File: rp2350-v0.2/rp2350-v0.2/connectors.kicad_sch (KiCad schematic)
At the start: 6 parts, among them J1 USB_C_Receptacle_USB2.0_14P, J2 SWD, J3 BAT, J5 DBG_UART

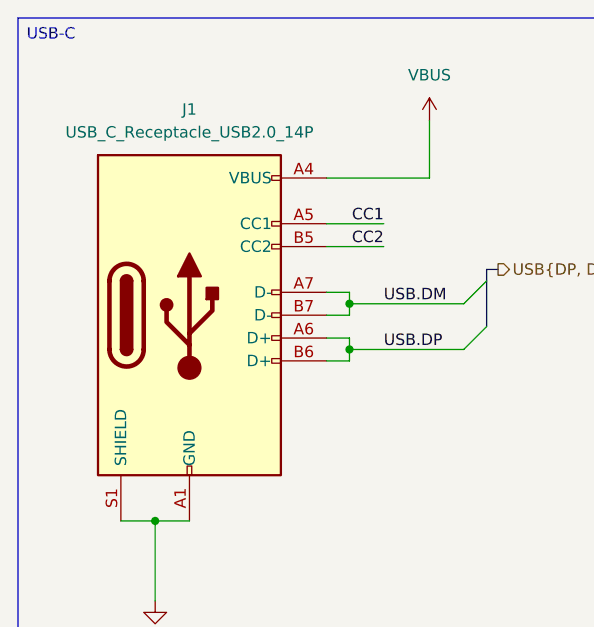
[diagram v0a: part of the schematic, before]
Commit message: v0.2: schematic draft 1 done
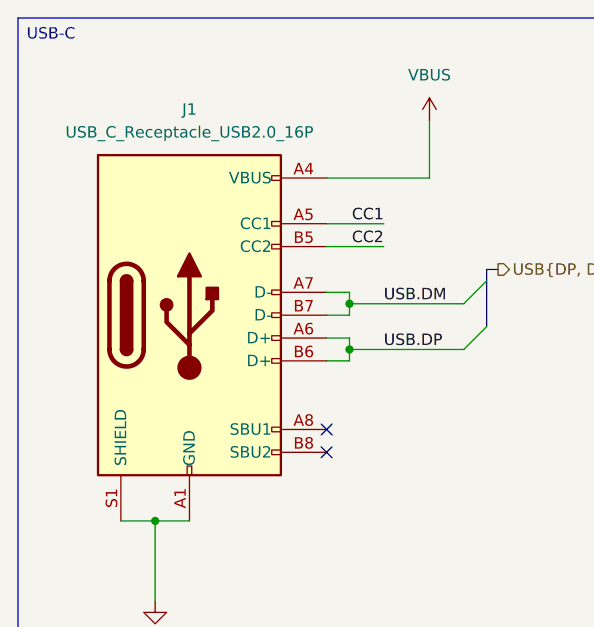
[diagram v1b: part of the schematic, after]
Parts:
- removed J1: USB_C_Receptacle_USB2.0_14P, symbol Connector:USB_C_Receptacle_USB2.0_14P
- added J1: USB_C_Receptacle_USB2.0_16P, CustomFootprints:GCT_USB4215_03_A, symbol Connector:USB_C_Receptacle_USB2.0_16P
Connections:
- net CC1: now also J1.A5 (CC1)
- net CC2: now also J1.B5 (CC2)
- net GND: now also J1.A1 (GND), J1.A12 (GND), J1.B1 (GND), J1.B12 (GND), J1.S1 (SHIELD)
- net USB.DM: now also J1.A7 (D-), J1.B7 (D-)
- net USB.DP: now also J1.A6 (D+), J1.B6 (D+)
- net VBUS: now also J1.A4 (VBUS), J1.A9 (VBUS), J1.B4 (VBUS), J1.B9 (VBUS)
- no-connect marks 0 -> 2
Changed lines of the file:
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@@
 		(color 0 0 0 0)
+	)
+	(no_connect
+		(at 96.52 81.28)
+	)
+	(no_connect
+		(at 96.52 83.82)
 	)
 	(bus_entry
@@
 	)
 	(symbol
+		(lib_id "Connector:USB_C_Receptacle_USB2.0_16P")
+		(at 81.28 68.58 0)
+		(unit 1)
+		(exclude_from_sim no)
+		(in_bom yes)
+		(on_board yes)
+		(dnp no)
+		(fields_autoplaced yes)
+		(property "Reference" "J1"
+			(at 81.28 45.72 0)
+			(effects
+				(font
+					(size 1.27 1.27)
+				)
+			)
+		)
+		(property "Value" "USB_C_Receptacle_USB2.0_16P"
+			(at 81.28 48.26 0)
+			(effects
+				(font
+					(size 1.27 1.27)
+				)
+			)
+		)
+		(property "Footprint" "CustomFootprints:GCT_USB4215_03_A"
+			(at 85.09 68.58 0)
+			(effects
+				(font
+					(size 1.27 1.27)
+				)
+				(hide yes)
+			)
+		)
+		(property "Datasheet" "https://www.usb.org/sites/default/files/documents/usb_type-c.zip"
+			(at 85.09 68.58 0)
+			(effects
+				(font
+					(size 1.27 1.27)
+				)
+				(hide yes)
+			)
+		)
+		(property "Description" "USB 2.0-only 16P Type-C Receptacle connector"
+			(at 81.28 68.58 0)
+			(effects
+				(font
+					(size 1.27 1.27)
+				)
+				(hide yes)
+			)
+		)
+		(pin "A5"
+		)
+		(pin "B8"
+		)
+		(pin "B6"
+		)
+		(pin "A8"
+		)
+		(pin "B12"
+		)
+		(pin "A7"
+		)
+		(pin "A12"
+		)
+		(pin "S1"
+		)
+		(pin "B4"
+		)
+		(pin "A6"
+		)
+		(pin "A9"
+		)
+		(pin "A4"
+		)
+		(pin "A1"
+		)
+		(pin "B1"
+		)
+		(pin "B9"
+		)
+		(pin "B7"
+		)
+		(pin "B5"
+		)
+		(instances
+			(project ""
+				(path "/5cbb45d4-7f83-48dd-a53b-5c75c7d1d827/a0109155-cd66-4000-9716-f8f6190d36bf"
+					(reference "J1")
+					(unit 1)
+				)
+			)
+		)
+	)
+	(symbol
 		(lib_id "Connector_Generic:Conn_01x03")
 		(at 167.64 63.5 180)
@@
 					(unit 1)
 				)
-			)
-		)
-	)
-	(symbol
-		(lib_id "Connector:USB_C_Receptacle_USB2.0_14P")
-		(at 81.28 68.58 0)
-		(unit 1)
-		(exclude_from_sim no)
-		(in_bom yes)
-		(on_board yes)
-		(dnp no)
-		(fields_autoplaced yes)
-		(property "Reference" "J1"
-			(at 81.28 45.72 0)
-			(effects
-				(font
-					(size 1.27 1.27)
-				)
-			)
-		)
-		(property "Value" "USB_C_Receptacle_USB2.0_14P"
-			(at 81.28 48.26 0)
-			(effects
-				(font
-					(size 1.27 1.27)
-				)
-			)
-		)
-		(property "Footprint" ""
-			(at 85.09 68.58 0)
-			(effects
-				(font
-					(size 1.27 1.27)
-				)
-				(hide yes)
-			)
-		)
-		(property "Datasheet" "https://www.usb.org/sites/default/files/documents/usb_type-c.zip"
-			(at 85.09 68.58 0)
-			(effects
-				(font
-					(size 1.27 1.27)
-				)
-				(hide yes)
-			)
-		)
-		(property "Description" "USB 2.0-only 14P Type-C Receptacle connector"
-			(at 81.28 68.58 0)
-			(effects
-				(font
-					(size 1.27 1.27)
-				)
-				(hide yes)
-			)
-		)
-		(pin "B1"
-		)
-		(pin "A12"
-		)
-		(pin "A7"
-		)
-		(pin "A9"
-		)
-		(pin "A5"
-		)
-		(pin "B5"
-		)
-		(pin "B9"
-		)
-		(pin "A6"
-		)
-		(pin "B12"
-		)
-		(pin "A1"
-		)
-		(pin "B4"
-		)
-		(pin "B6"
-		)
-		(pin "S1"
-		)
-		(pin "B7"
-		)
-		(pin "A4"
-		)
-		(instances
-			(project "rp2350-v0.2"
-				(path "/5cbb45d4-7f83-48dd-a53b-5c75c7d1d827/a0109155-cd66-4000-9716-f8f6190d36bf"
-					(reference "J1")
-					(unit 1)
-				)

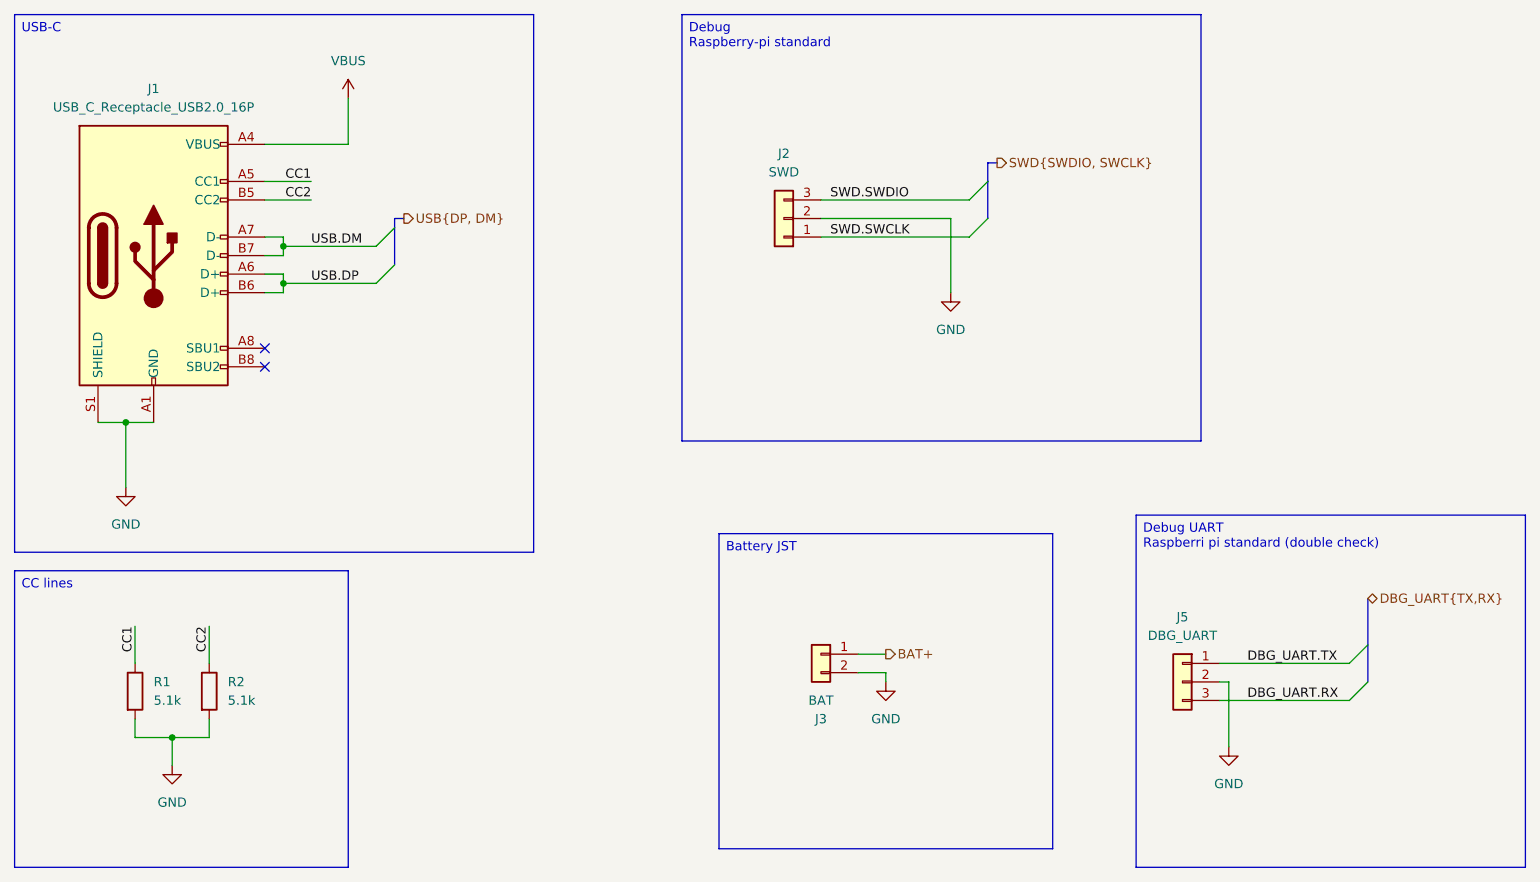
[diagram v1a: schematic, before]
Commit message: v0.2: more progress on routing, nearly done
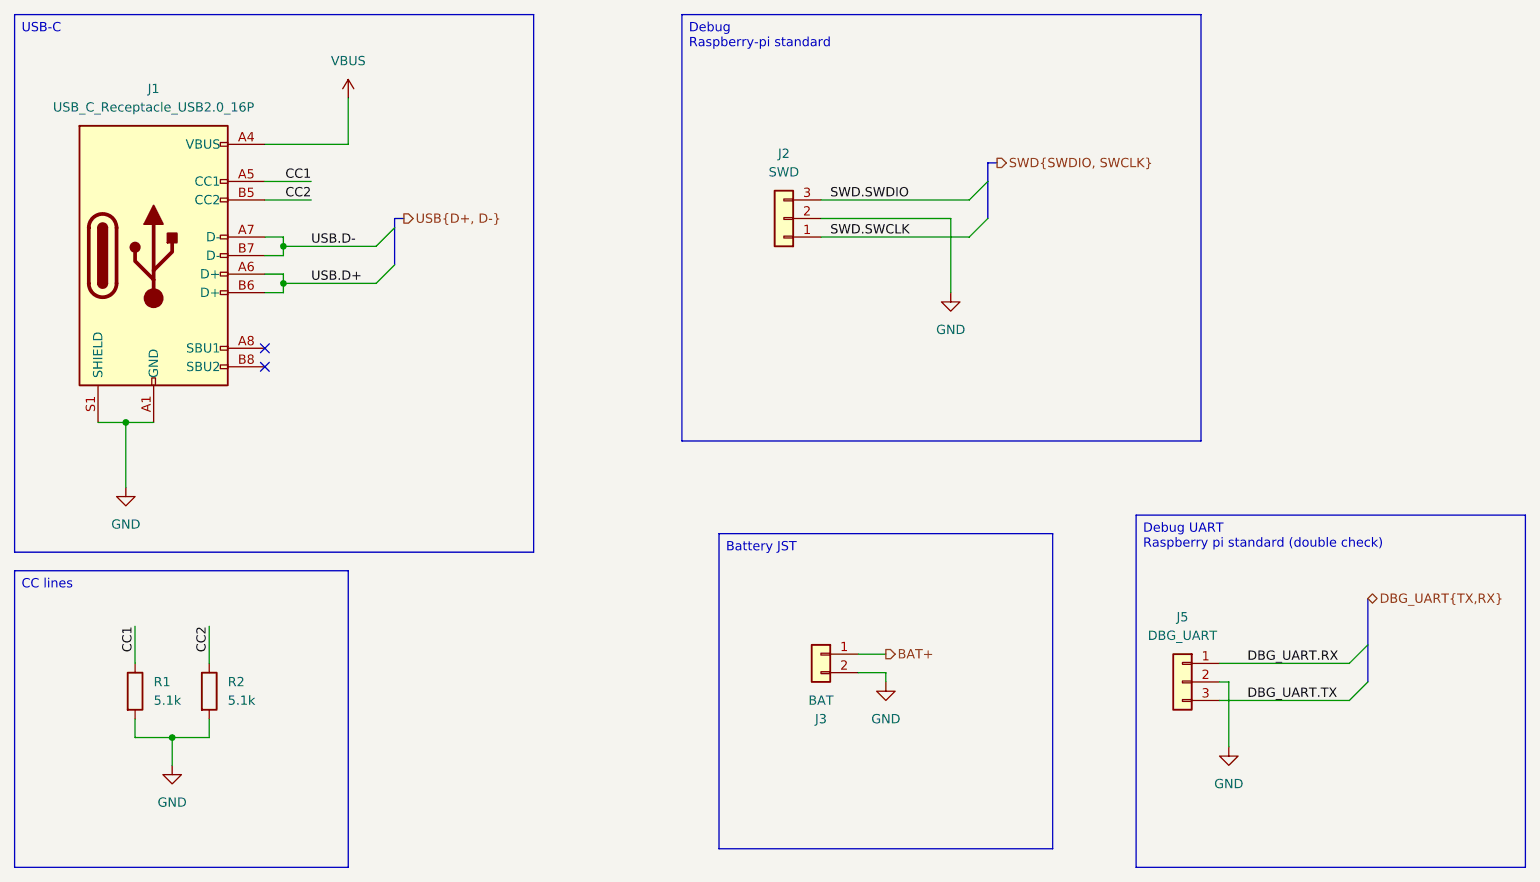
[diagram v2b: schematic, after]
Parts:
- J2, J5: footprint Connector_PinHeader_2.54mm:PinHeader_1x03_P2.54mm_Vertical -> Connector_JST:JST_SH_SM03B-SRSS-TB_1x03-1MP_P1.00mm_Horizontal
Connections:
- net DBG_UART.RX: now also J5.1 (Pin_1); no longer J5.3 (Pin_3)
- net DBG_UART.TX: now also J5.3 (Pin_3); no longer J5.1 (Pin_1)
- net USB.DM renamed USB.D-
- net USB.DP renamed USB.D+
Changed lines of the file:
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@@
 	(generator_version "9.0")
 	(paper "A4")
-	(text_box "Debug UART\nRaspberri pi standard (double check)"
+	(text_box "Debug UART\nRaspberry pi standard (double check)"
 		(exclude_from_sim no)
 		(at 215.9 104.14 0)
@@
 		)
 	)
-	(label "USB.DM"
+	(label "DBG_UART.TX"
+		(at 231.14 129.54 0)
+		(effects
+			(font
+				(size 1.27 1.27)
+			)
+			(justify left bottom)
+		)
+	)
+	(label "USB.D-"
 		(at 102.87 67.31 0)
 		(effects
@@
 		)
 	)
-	(label "DBG_UART.RX"
-		(at 231.14 129.54 0)
-		(effects
-			(font
-				(size 1.27 1.27)
-			)
-			(justify left bottom)
-		)
-	)
 	(label "CC2"
 		(at 88.9 119.38 270)
@@
 		)
 	)
+	(label "DBG_UART.RX"
+		(at 231.14 124.46 0)
+		(effects
+			(font
+				(size 1.27 1.27)
+			)
+			(justify left bottom)
+		)
+	)
 	(label "CC1"
 		(at 78.74 119.38 270)
@@
 		)
 	)
-	(label "DBG_UART.TX"
-		(at 231.14 124.46 0)
-		(effects
-			(font
-				(size 1.27 1.27)
-			)
-			(justify left bottom)
-		)
-	)
 	(label "CC2"
 		(at 102.87 60.96 180)
@@
 		)
 	)
-	(label "USB.DP"
+	(label "USB.D+"
 		(at 102.87 72.39 0)
 		(effects
@@
 		)
 	)
-	(hierarchical_label "USB{DP, DM}"
+	(hierarchical_label "USB{D+, D-}"
 		(shape output)
 		(at 115.57 63.5 0)
@@
 			)
 		)
-		(property "Footprint" "Connector_PinHeader_2.54mm:PinHeader_1x03_P2.54mm_Vertical"
+		(property "Footprint" "Connector_JST:JST_SH_SM03B-SRSS-TB_1x03-1MP_P1.00mm_Horizontal"
 			(at 222.25 127 0)
 			(effects
@@
 			)
 		)
-		(property "Footprint" "Connector_PinHeader_2.54mm:PinHeader_1x03_P2.54mm_Vertical"
+		(property "Footprint" "Connector_JST:JST_SH_SM03B-SRSS-TB_1x03-1MP_P1.00mm_Horizontal"
 			(at 167.64 63.5 0)
 			(effects

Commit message: v0.2: final big checks done, fixed IrDA footprint
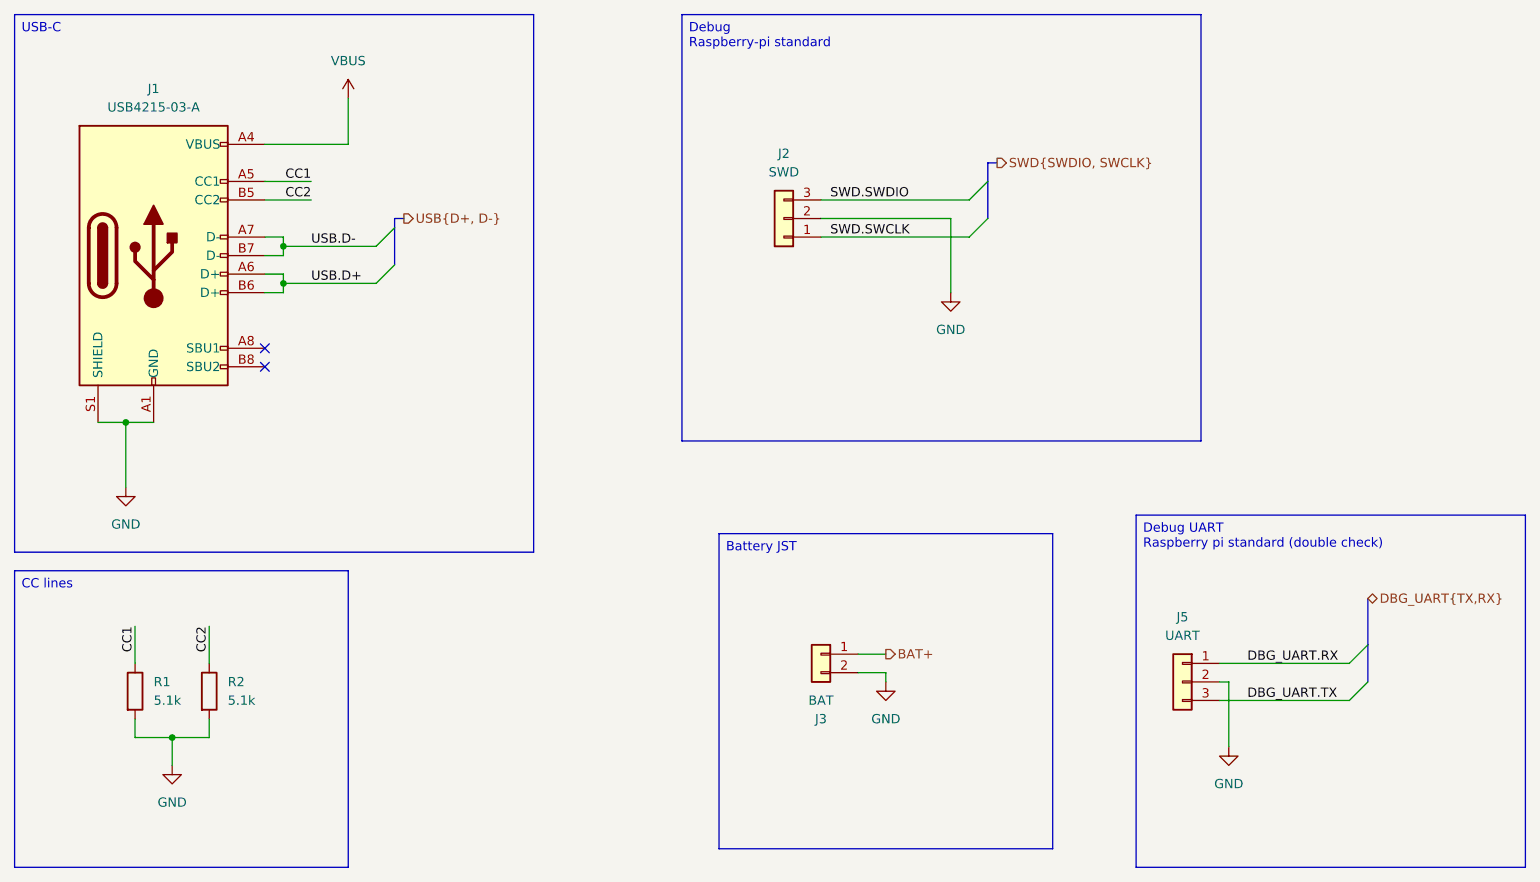
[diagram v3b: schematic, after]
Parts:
- J1: value USB_C_Receptacle_USB2.0_16P -> USB4215-03-A
- J5: value DBG_UART -> UART
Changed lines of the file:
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@@
 			)
 		)
-		(property "Value" "DBG_UART"
+		(property "Value" "UART"
 			(at 222.25 120.65 0)
 			(effects
@@
 			)
 		)
-		(property "Value" "USB_C_Receptacle_USB2.0_16P"
+		(property "Value" "USB4215-03-A"
 			(at 81.28 48.26 0)
 			(effects

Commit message: v0.2: update battery connector and labels
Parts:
- J3: footprint Connector_JST:JST_PH_B2B-PH-K_1x02_P2.00mm_Vertical -> Connector_JST:JST_PH_S2B-PH-K_1x02_P2.00mm_Horizontal
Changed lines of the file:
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@@
 			)
 		)
-		(property "Footprint" "Connector_JST:JST_PH_B2B-PH-K_1x02_P2.00mm_Vertical"
+		(property "Footprint" "Connector_JST:JST_PH_S2B-PH-K_1x02_P2.00mm_Horizontal"
 			(at 172.72 123.19 0)
 			(effects
